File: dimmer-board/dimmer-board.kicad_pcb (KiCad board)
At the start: 2 copper layers, 38.7 x 50.8 mm, 16 parts, among them J1 Conn_01x03_Pin, J2 Conn_01x05_Pin, J3 Screw_Terminal_01x02, J5 Screw_Terminal_01x04, Q1 ME60N03, Q2 ME60N03

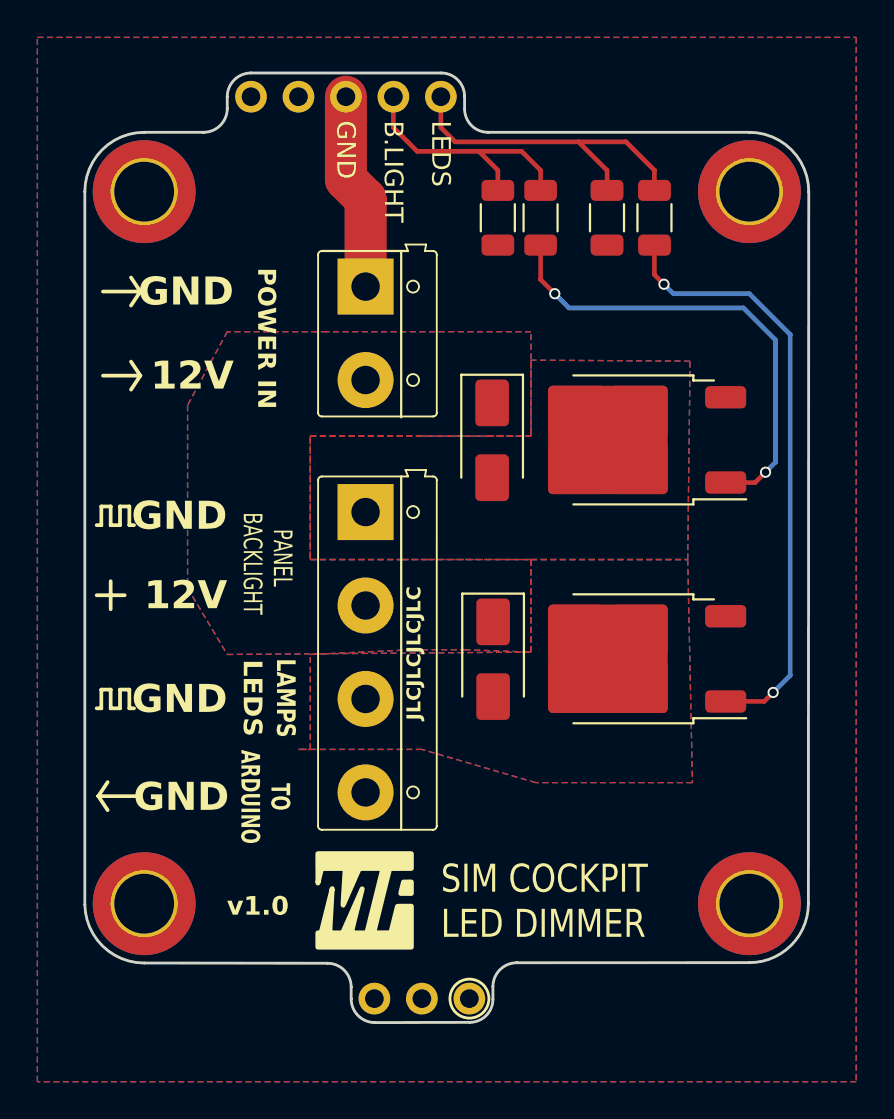
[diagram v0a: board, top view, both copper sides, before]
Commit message: update dimmer board to KiCad version 9
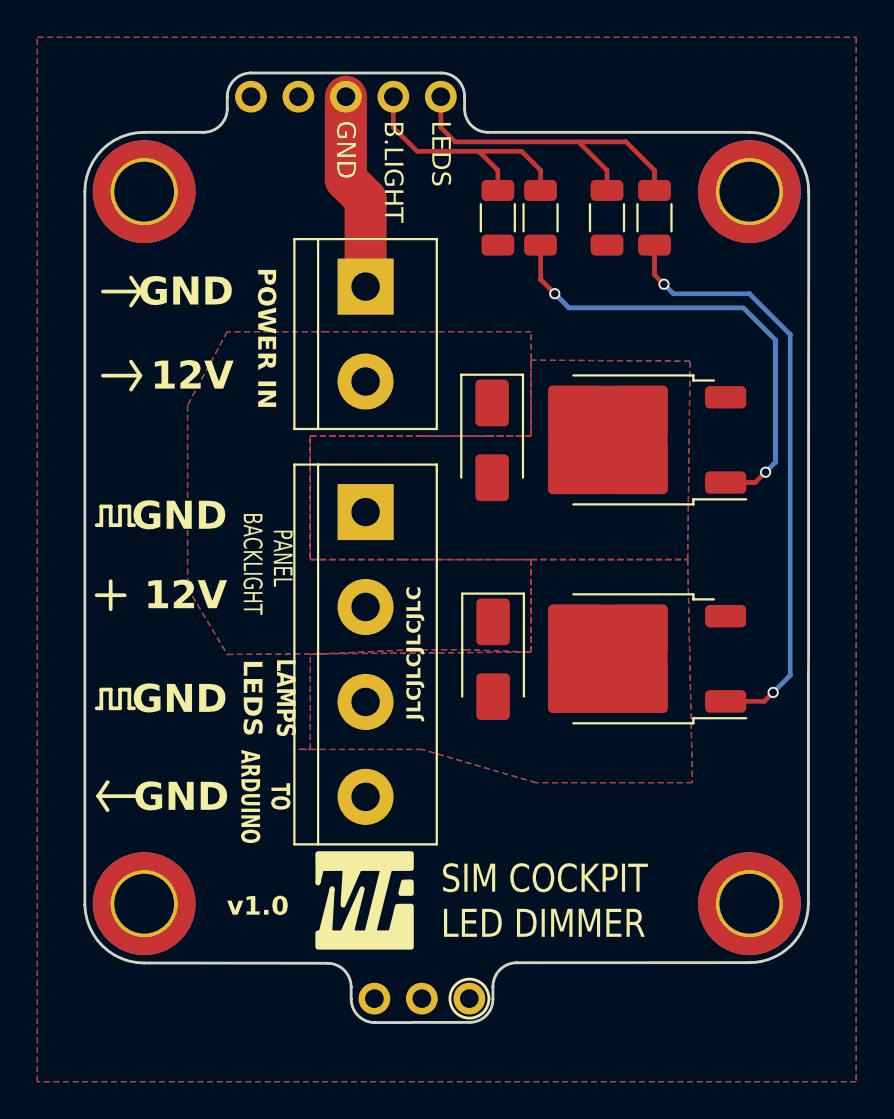
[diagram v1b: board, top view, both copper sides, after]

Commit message: update symbols on dimmer board, fixed DRC
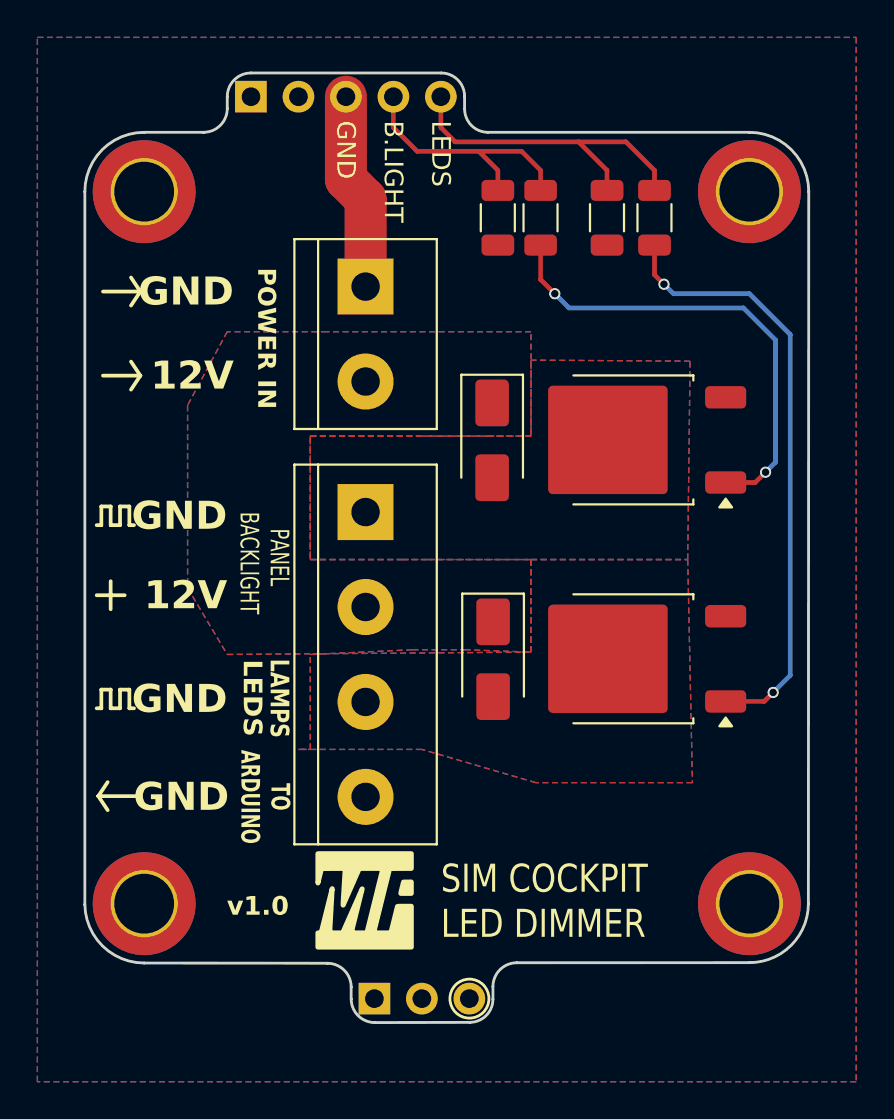
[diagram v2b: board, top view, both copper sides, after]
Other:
- board text removed: "JLCJLCJLCJLC"

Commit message: use screw terminals from MF lib
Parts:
- J3: footprint TerminalBlock:TerminalBlock_bornier-2_P5.08mm -> MobiFlight:TerminalBlock_bornier-2_P5.08mm
- J5: footprint TerminalBlock:TerminalBlock_bornier-4_P5.08mm -> MobiFlight:TerminalBlock_bornier-4_P5.08mm
